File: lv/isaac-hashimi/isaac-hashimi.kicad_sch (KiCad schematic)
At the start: 0 parts

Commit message: Add brake pressure comparator
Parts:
- added C1: 100nf, symbol Device:C
- added R1, R2, R3: R, Resistor_THT:R_Array_SIP4, symbol Device:R
- added U1: LMV393, Package_TO_SOT_SMD:SOT-23-5, symbol Comparator:LMV393
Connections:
- new net: R1.2, R2.1, U1.2 (-)
- new net +5V: C1.1, R1.1, R3.1, U1.8 (V+)
- new net Brake_High: R3.2, U1.1
- new net Brake_Pressure: U1.3 (+)
- new net GND: C1.2, R2.2, U1.4 (V-)

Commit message: Finish brake pressure comparator
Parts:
- R1: value R -> 19.6k
- R2, R3: value R -> 10k
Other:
- moved on the sheet: C1, R1, R2, R3, U1A, U1C

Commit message: Add current comparator
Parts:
- added R4: 8.45k, Resistor_THT:R_Array_SIP4, symbol Device:R
- added R5, R6: 10k, Resistor_THT:R_Array_SIP4, symbol Device:R
- added unit 2 of U1
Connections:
- net +5V: now also R4.1, R6.1
- net GND: now also R5.2
- new net: R4.2, R5.1, U1.6 (-)
- new net Current_High: R6.2, U1.7
- new net Current_Sense: U1.5 (+)

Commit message: Wire-AND comparator outputs
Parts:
- removed R3: 10k, Resistor_THT:R_Array_SIP4, symbol Device:R
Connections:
- net Current_High is gone; now on net Plausibility_Fault: R6.2, U1.7
- net Brake_High renamed Plausibility_Fault
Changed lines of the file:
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@@
 		(color 0 0 0 0)
 	)
+	(junction
+		(at 448.31 281.94)
+		(diameter 0)
+		(color 0 0 0 0)
+	)
 	(wire
 		(pts
@@
 	(wire
 		(pts
-			(xy 443.23 281.94) (xy 453.39 281.94)
+			(xy 443.23 281.94) (xy 448.31 281.94)
 		)
 		(stroke
@@
 	(wire
 		(pts
+			(xy 448.31 281.94) (xy 453.39 281.94)
+		)
+		(stroke
+			(width 0)
+			(type default)
+		)
+	)
+	(wire
+		(pts
 			(xy 402.59 284.48) (xy 427.99 284.48)
 		)
@@
 	(wire
 		(pts
+			(xy 448.31 175.26) (xy 448.31 281.94)
+		)
+		(stroke
+			(width 0)
+			(type default)
+		)
+	)
+	(wire
+		(pts
 			(xy 373.38 151.13) (xy 373.38 157.48)
 		)
@@
 	(wire
 		(pts
-			(xy 443.23 175.26) (xy 478.79 175.26)
+			(xy 443.23 175.26) (xy 448.31 175.26)
 		)
 		(stroke
@@
 	(wire
 		(pts
-			(xy 478.79 175.26) (xy 478.79 143.51)
-		)
-		(stroke
-			(width 0)
-			(type default)
-		)
-	)
-	(wire
-		(pts
 			(xy 453.39 266.7) (xy 453.39 270.51)
 		)
@@
 			(width 0)
 			(type default)
-		)
-	)
-	(wire
-		(pts
-			(xy 478.79 120.65) (xy 478.79 135.89)
-		)
-		(stroke
-			(width 0)
-			(type default)
-		)
-	)
-	(label "Brake_High"
-		(at 478.79 172.72 0)
-		(effects
-			(font
-				(size 1.27 1.27)
-			)
-			(justify left bottom)
 		)
 	)
@@
 		)
 	)
-	(label "Current_High"
+	(label "Plausibility_Fault"
 		(at 453.39 281.94 0)
+		(effects
+			(font
+				(size 1.27 1.27)
+			)
+			(justify left bottom)
+		)
+	)
+	(label "Plausibility_Fault"
+		(at 448.31 185.42 0)
 		(effects
 			(font
@@
 	)
 	(symbol
-		(lib_id "power:+5V")
-		(at 478.79 120.65 0)
-		(unit 1)
-		(body_style 1)
-		(exclude_from_sim no)
-		(in_bom yes)
-		(on_board yes)
-		(in_pos_files yes)
-		(dnp no)
-		(fields_autoplaced yes)
-		(property "Reference" "#PWR02"
-			(at 478.79 124.46 0)
-			(hide yes)
-			(show_name no)
-			(do_not_autoplace no)
-			(effects
-				(font
-					(size 1.27 1.27)
-				)
-			)
-		)
-		(property "Value" "+5V"
-			(at 478.79 115.57 0)
-			(show_name no)
-			(do_not_autoplace no)
-			(effects
-				(font
-					(size 1.27 1.27)
-				)
-			)
-		)
-		(property "Footprint" ""
-			(at 478.79 120.65 0)
-			(hide yes)
-			(show_name no)
-			(do_not_autoplace no)
-			(effects
-				(font
-					(size 1.27 1.27)
-				)
-			)
-		)
-		(property "Datasheet" ""
-			(at 478.79 120.65 0)
-			(hide yes)
-			(show_name no)
-			(do_not_autoplace no)
-			(effects
-				(font
-					(size 1.27 1.27)
-				)
-			)
-		)
-		(property "Description" "Power symbol creates a global label with name \"+5V\""
-			(at 478.79 120.65 0)
-			(hide yes)
-			(show_name no)
-			(do_not_autoplace no)
-			(effects
-				(font
-					(size 1.27 1.27)
-				)
-			)
-		)
-		(pin "1"
-		)
-		(instances
-			(project "isaac-hashimi"
-				(path "/e994741c-7c7d-4124-9d00-43b883baa61d"
-					(reference "#PWR02")
-					(unit 1)
-				)
-			)
-		)
-	)
-	(symbol
 		(lib_id "Device:C")
 		(at 406.4 185.42 0)
@@
 					(unit 1)
 				)
-			)
-		)
-	)
-	(symbol
-		(lib_id "Device:R")
-		(at 478.79 139.7 0)
-		(unit 1)
-		(body_style 1)
-		(exclude_from_sim no)
-		(in_bom yes)
-		(on_board yes)
-		(in_pos_files yes)
-		(dnp no)
-		(fields_autoplaced yes)
-		(property "Reference" "R3"
-			(at 481.33 138.4299 0)
-			(show_name no)
-			(do_not_autoplace no)
-			(effects
-				(font
-					(size 1.27 1.27)
-				)
-				(justify left)
-			)
-		)
-		(property "Value" "10k"
-			(at 481.33 140.9699 0)
-			(show_name no)
-			(do_not_autoplace no)
-			(effects
-				(font
-					(size 1.27 1.27)
-				)
-				(justify left)
-			)
-		)
-		(property "Footprint" "Resistor_THT:R_Array_SIP4"
-			(at 477.012 139.7 90)
-			(hide yes)
-			(show_name no)
-			(do_not_autoplace no)
-			(effects
-				(font
-					(size 1.27 1.27)
-				)
-			)
-		)
-		(property "Datasheet" ""
-			(at 478.79 139.7 0)
-			(hide yes)
-			(show_name no)
-			(do_not_autoplace no)
-			(effects
-				(font
-					(size 1.27 1.27)
-				)
-			)
-		)
-		(property "Description" "Resistor"
-			(at 478.79 139.7 0)
-			(hide yes)
-			(show_name no)
-			(do_not_autoplace no)
-			(effects
-				(font
-					(size 1.27 1.27)
-				)
-			)
-		)
-		(property "Digikey Part Number" ""
-			(at 478.79 139.7 0)
-			(hide yes)
-			(show_name no)
-			(do_not_autoplace no)
-			(effects
-				(font
-					(size 1.27 1.27)
-				)
-			)
-		)
-		(property "Digikey URL" ""
-			(at 478.79 139.7 0)
-			(hide yes)
-			(show_name no)
-			(do_not_autoplace no)
-			(effects
-				(font
-					(size 1.27 1.27)
-				)
-			)
-		)
-		(property "Manufacturer" ""
-			(at 478.79 139.7 0)
-			(hide yes)
-			(show_name no)
-			(do_not_autoplace no)
-			(effects
-				(font
-					(size 1.27 1.27)
-				)
-			)
-		)
-		(property "Manufacturer Part Number" ""
-			(at 478.79 139.7 0)
-			(hide yes)
-			(show_name no)
-			(do_not_autoplace no)
-			(effects
-				(font
-					(size 1.27 1.27)
-				)
-			)
-		)
-		(pin "2"
-		)
-		(pin "1"
-		)
-		(instances
-			(project "isaac-hashimi"
-				(path "/e994741c-7c7d-4124-9d00-43b883baa61d"
-					(reference "R3")
-					(unit 1)
-				)

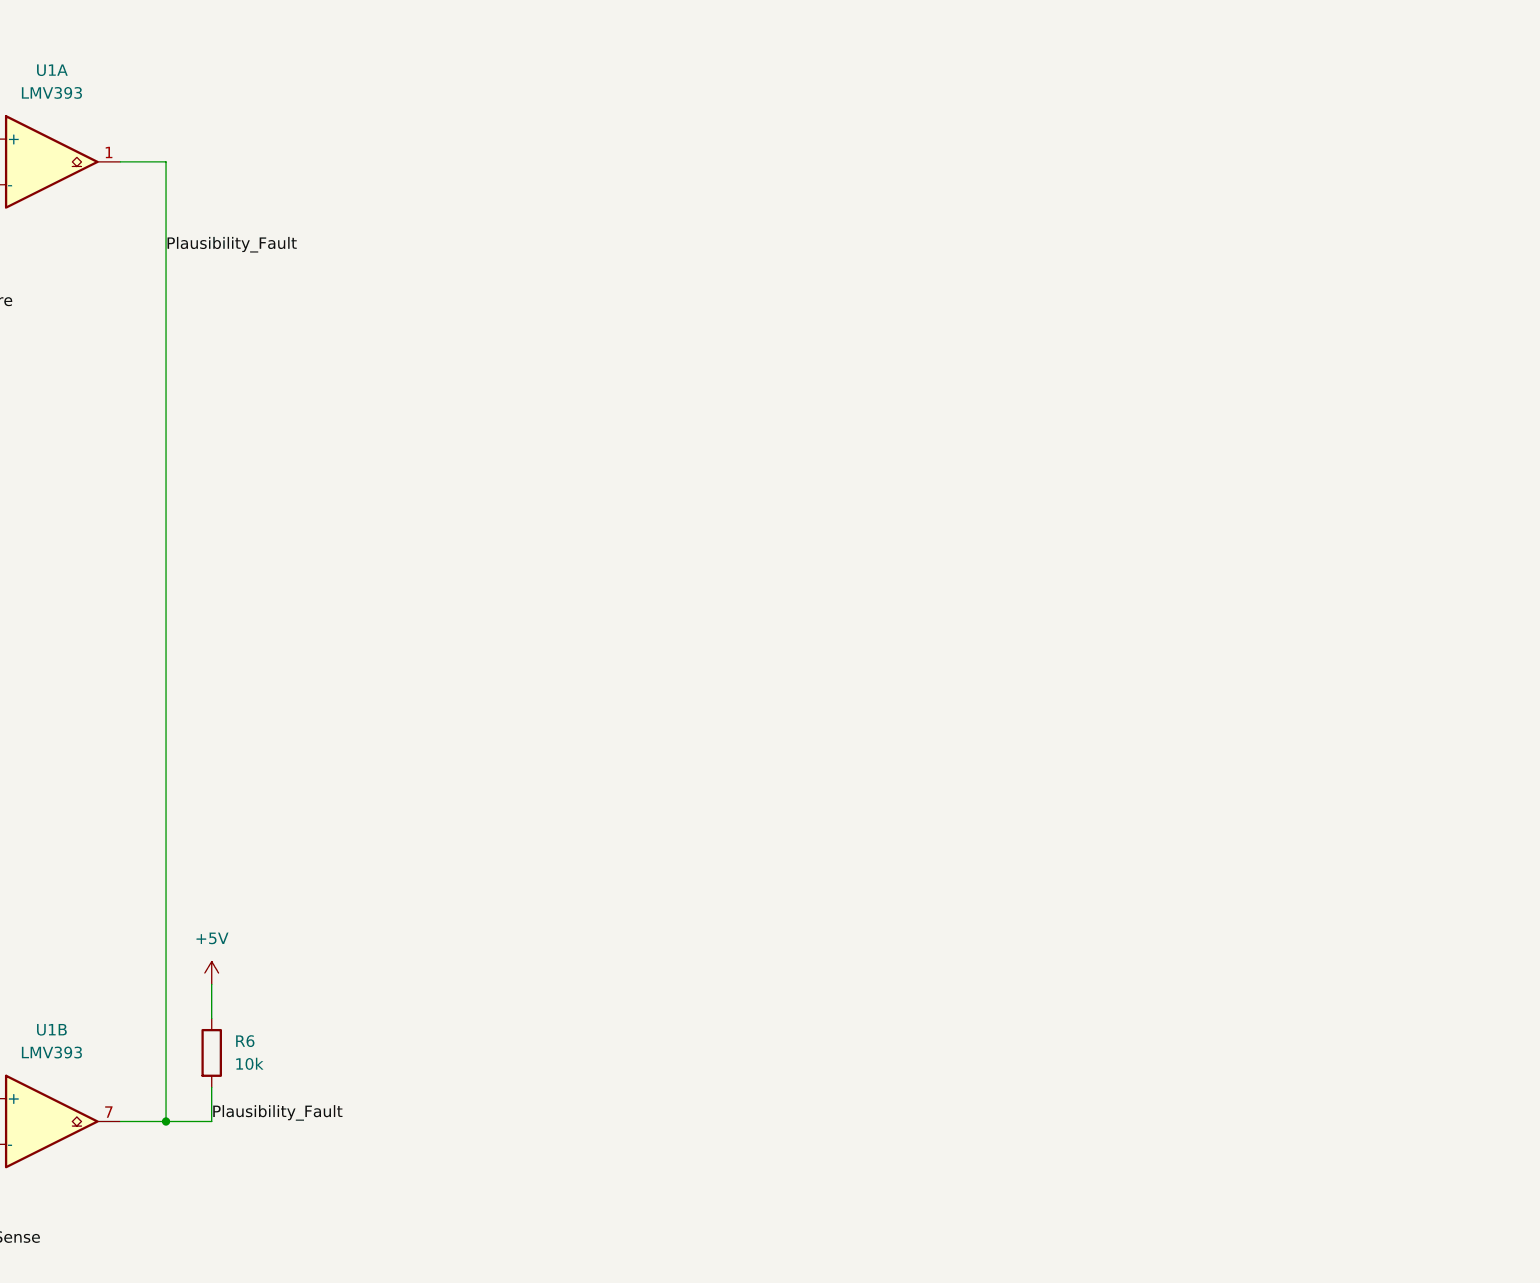
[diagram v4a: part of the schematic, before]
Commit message: Add 500 ms delay block
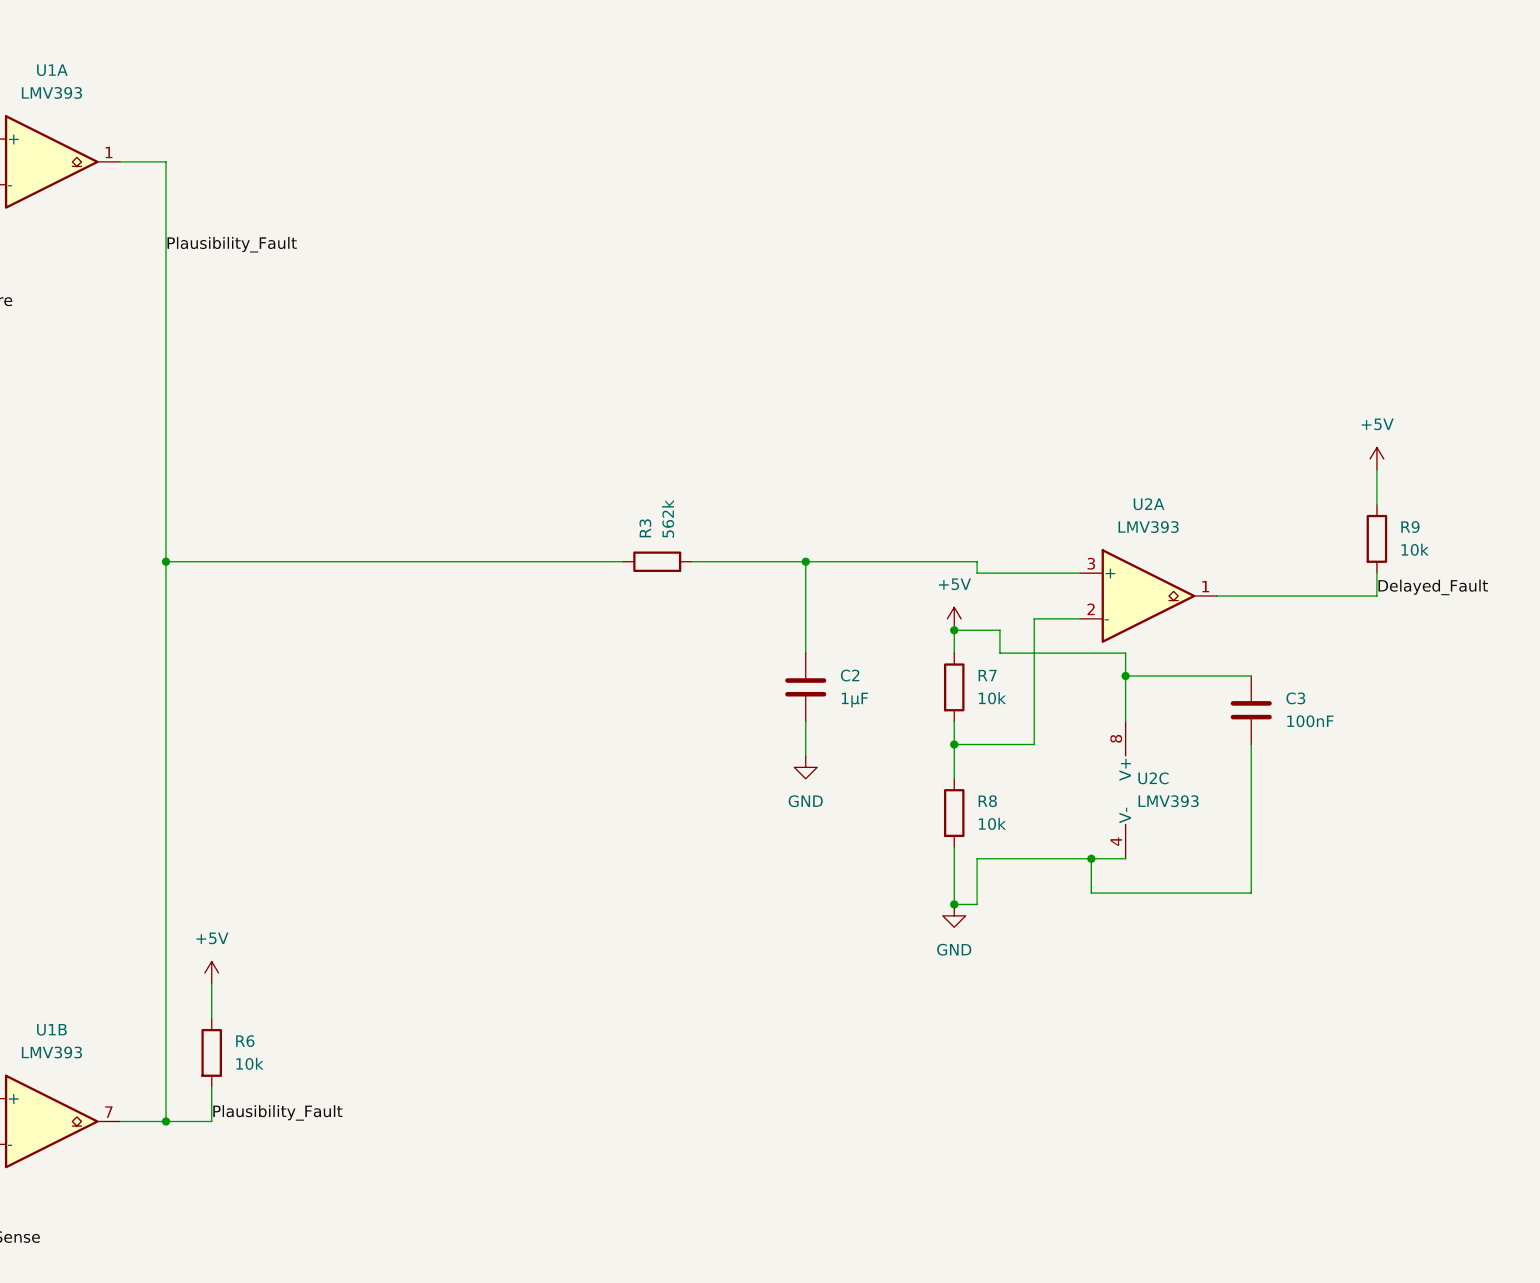
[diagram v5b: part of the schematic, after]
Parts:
- added C2: 1µF, Package_SO:SOIC-8_3.9x4.9mm_P1.27mm, symbol Device:C
- added C3: 100nF, Package_SO:SOIC-8_3.9x4.9mm_P1.27mm, symbol Device:C
- added R3: 562k, Resistor_THT:R_Array_SIP4, symbol Device:R
- added R7: 10k, Resistor_THT:R_Array_SIP4, symbol Device:R
- added R8, R9: 10k, symbol Device:R
- added U2: LMV393, symbol Comparator:LMV393
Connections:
- net +5V: now also C3.1, R7.1, R9.1, U2.8 (V+)
- net GND: now also C2.2, C3.2, R8.2, U2.4 (V-)
- net Plausibility_Fault: now also R3.1
- new net: R7.2, R8.1, U2.2 (-)
- new net: C2.1, R3.2, U2.3 (+)
- new net Delayed_Fault: R9.2, U2.1

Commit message: Add latch
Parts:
- added D1: 1N4148, symbol Device:D
- added R10: 100k, symbol Device:R
- added R11, R12: 10k, symbol Device:R
- added unit 2 of U2
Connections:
- net +5V: now also R11.1
- net Delayed_Fault: now also D1.2 (A)
- net GND: now also R10.2
- new net: D1.1 (K), R10.1, R12.1, U2.5 (+)
- new net BSPD_Trip: R11.2, R12.2, U2.7
- new net Ref_2V5: U2.6 (-)

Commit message: Add fail-safe relay output stage
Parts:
- added D2: 1N4148, symbol Device:D
- added K1: G5V-1, Relay_THT:Relay_SPDT_Omron_G5V-1, symbol Relay:G5V-1
- added Q1, Q2: 2N7002, Package_TO_SOT_SMD:SOT-23, symbol Transistor_FET:2N7002
- added R13: 10k, Package_TO_SOT_SMD:SOT-23, symbol Device:R
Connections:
- net +5V: now also D2.1 (K), K1.2, R13.1
- net BSPD_Trip: now also Q1.1 (G)
- net GND: now also Q1.2 (S), Q2.2 (S)
- new net: Q1.3 (D), Q2.1 (G), R13.2
- new net: D2.2 (A), K1.9, Q2.3 (D)
- new net SDC_IN: K1.1
- new net SDC_OUT: K1.5, K1.6
- no-connect marks 0 -> 1
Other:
- moved on the sheet: C1, C2, C3, D1, R1, R10, R11, R12, R2, R3, R4, R5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

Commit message: Complete sensor fault detection
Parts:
- added C4, C5: 100nf, symbol Device:C
- added D3: 1N4148, symbol Device:D
- added Q3: 2N7002, Package_TO_SOT_SMD:SOT-23, symbol Transistor_FET:2N7002
- added R14, R15: 10k, Package_TO_SOT_SMD:SOT-23, symbol Device:R
- added R16: 158K, Resistor_THT:R_Array_SIP4, symbol Device:R
- added R17, R18: 10k, Resistor_THT:R_Array_SIP4, symbol Device:R
- added R19: 158k, Resistor_THT:R_Array_SIP4, symbol Device:R
- added U3, U4: LMV393, symbol Comparator:LMV393
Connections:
- net +5V: now also C4.1, C5.1, R14.1, R15.1, R16.1, R18.1, U3.8 (V+), U4.8 (V+)
- net Brake_Pressure: now also U3.3 (+), U3.6 (-)
- net Current_Sense: now also U4.3 (+), U4.6 (-)
- net GND: now also C4.2, C5.2, Q3.2 (S), R17.2, R19.2, U3.4 (V-), U4.4 (V-)
- net Ref_2V5: now also R7.2, R8.1, U2.2 (-)
- net Latch_Node: now reaches D1.1 (K), R10.1, R12.1, U2.5 (+)
- net Latch_Node: now also D3.1 (K)
- new net 0.3V: R16.2, R17.1, U3.2 (-), U4.2 (-)
- new net 4.7V: R18.2, R19.1, U3.5 (+), U4.5 (+)
- new net Sensor_Fault: D3.2 (A), Q3.3 (D), R15.2
- new net Sensors_OK: Q3.1 (G), R14.2, U3.1, U3.7, U4.1, U4.7
